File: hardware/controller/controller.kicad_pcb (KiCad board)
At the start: 4 copper layers, 70 x 55 mm, 105 parts, among them SW1 EVP-ASAC1A, SW2 CL-SB-13A-02T, SW3 EVP-ASAC1A, SW4 EVP-ASAC1A, SW5 EVP-ASAC1A, SW6 EVP-ASAC1A, U1 EA8212HT6R, U2 MT3406, U3 XDJK-0051-025, U4 EMS4000RSW, U5 baochip1x, U6 EMS4000RSW, U7 baochip1x, Y1 48 MHz, Y2 48 MHz

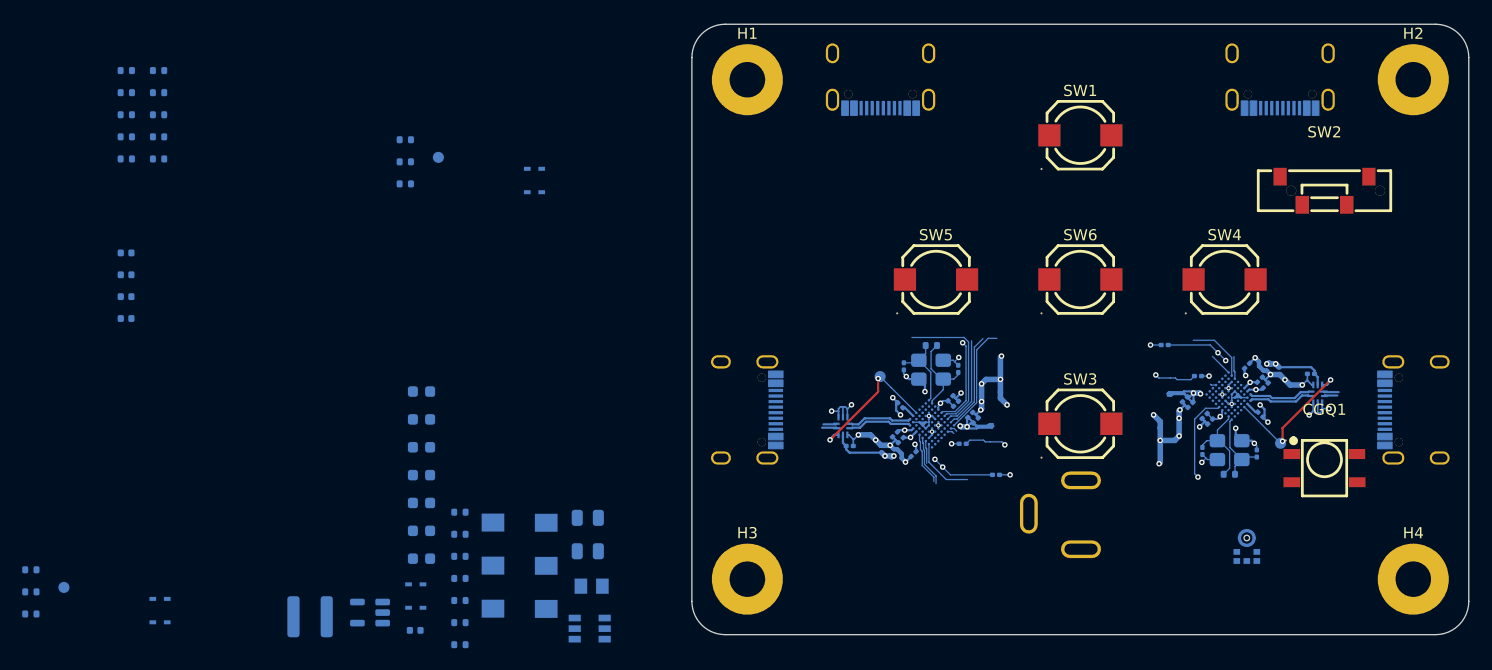
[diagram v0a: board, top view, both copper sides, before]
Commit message: placing power parts
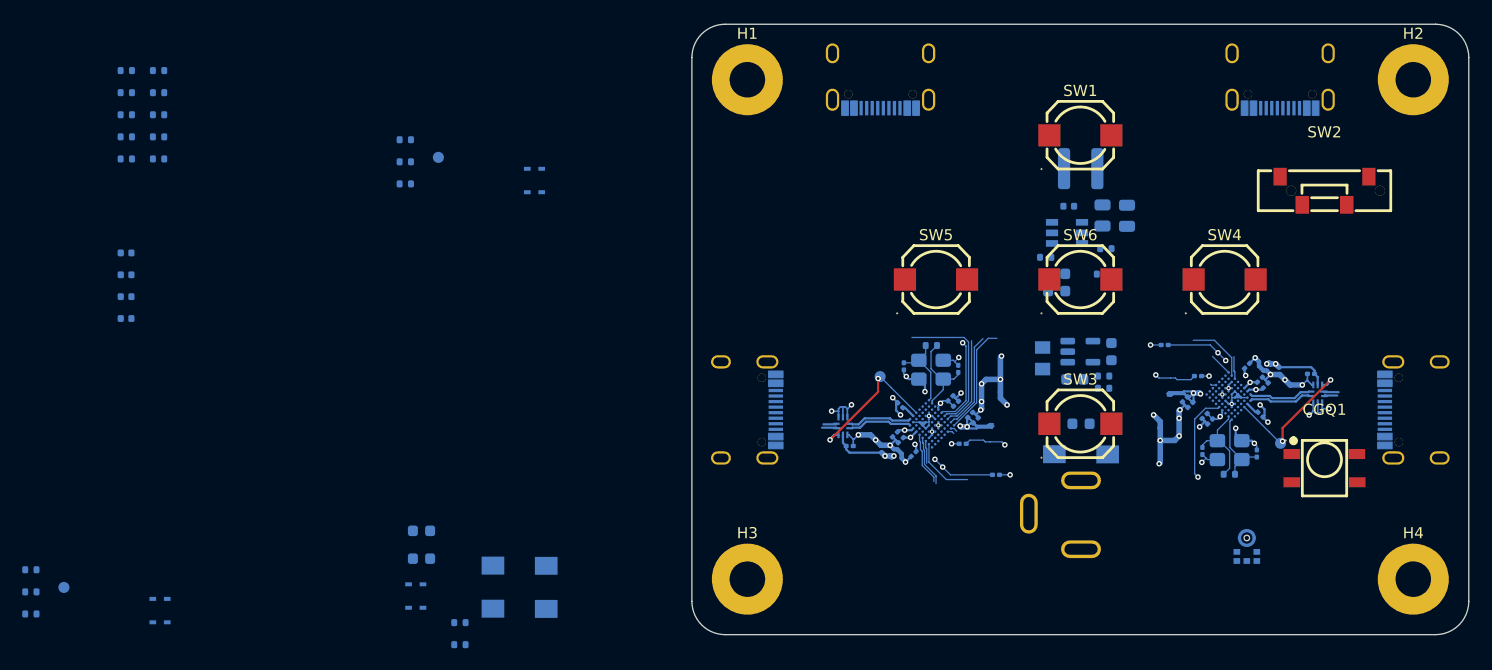
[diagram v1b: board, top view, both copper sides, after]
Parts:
- moved L2 80.3 mm to (135.0, 93.0), turned to 0 degrees
- moved C2 70.2 mm to (134.0, 96.4)
- moved U2 68.2 mm to (135.0, 109.5), turned to 0 degrees
- moved R2 63.6 mm to (137.3, 100.2), turned to 0 degrees
- moved C3 62.5 mm to (137.8, 109.5), turned to -90 degrees
- moved R1 61.7 mm to (137.0, 102.5), turned to 0 degrees
- moved R5 61.2 mm to (131.9, 101.0)
- moved R4 60.8 mm to (137.1, 111.7), turned to 0 degrees
- moved R3 59.9 mm to (137.1, 112.8)
- moved C8 59.8 mm to (135.1, 116.0), turned to 0 degrees
- moved C6 59.6 mm to (132.9, 104.0), turned to 0 degrees
- moved C4 59.3 mm to (132.9, 102.5), turned to 0 degrees
- moved C1 58.9 mm to (134.5, 112.0), turned to 0 degrees
- moved C7 57.2 mm to (139.2, 97.3), turned to -90 degrees
- moved U1 55.9 mm to (133.8, 98.8), turned to 0 degrees
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
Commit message: placing the remaining parts
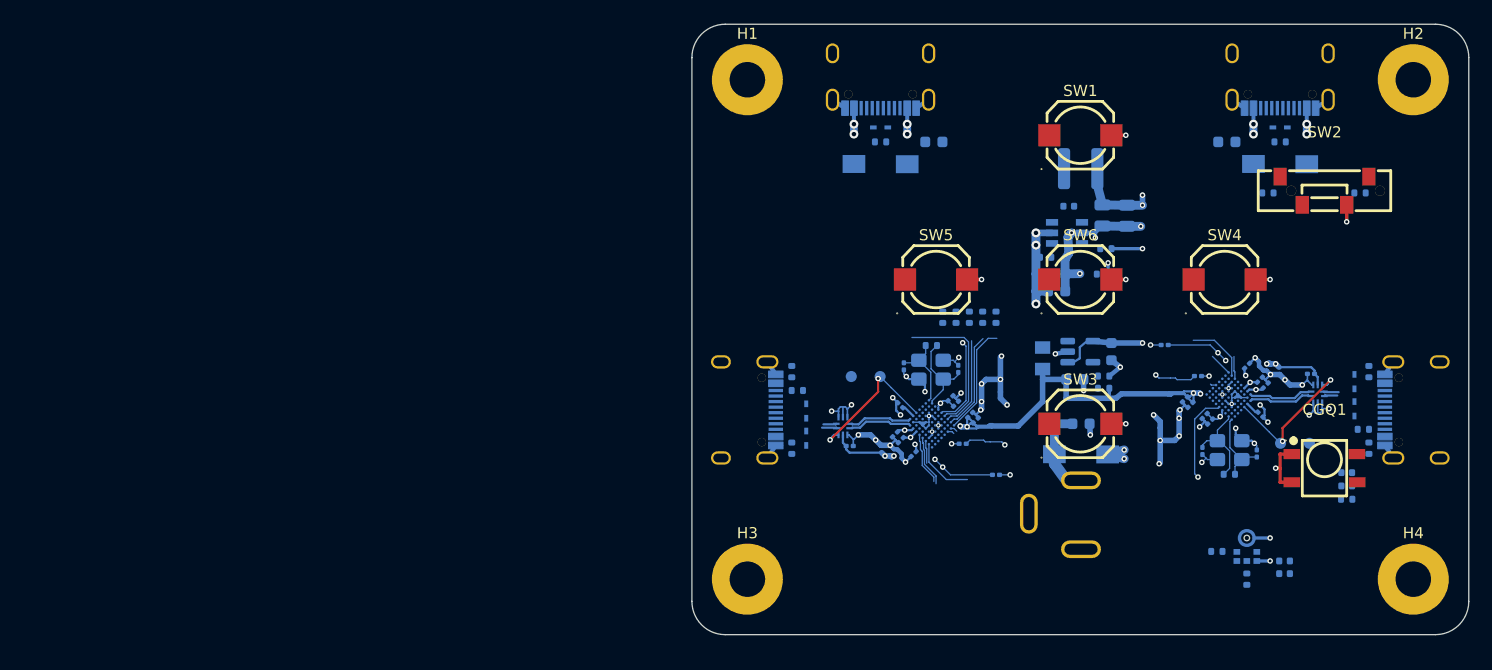
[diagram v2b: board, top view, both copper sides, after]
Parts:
- moved R20 115.3 mm to (159.0, 122.8)
- moved C37 111.1 mm to (159.0, 120.4)
- moved C38 111.0 mm to (159.0, 121.6), turned to 0 degrees
- moved R19 110.1 mm to (150.0, 130.0), turned to 90 degrees
- moved R25 108.5 mm to (160.2, 95.2)
- moved C35 108.3 mm to (153.4, 129.5), turned to 0 degrees
- moved C36 107.5 mm to (153.4, 128.4), turned to 0 degrees
- moved R18 107.4 mm to (147.3, 127.5), turned to 0 degrees
- moved R22 102.9 mm to (151.9, 95.2), turned to 0 degrees
- moved R15 91.2 mm to (161.0, 118.2), turned to 90 degrees
- moved R17 89.1 mm to (160.5, 116.5), turned to 0 degrees
- moved D4 89.1 mm to (153.0, 89.3)
- moved R16 88.9 mm to (161.0, 111.3), turned to -90 degrees
- moved R7 86.7 mm to (153.0, 90.6), turned to 0 degrees
- moved TP4 82.6 mm to (155.6, 117.8)
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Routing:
- net GND: track 78.1 -> 124.5 mm, vias 40 -> 58
- net +12V: track 0.00 -> 26.6 mm, vias 0 -> 11
- net +0.85V: track 30.0 -> 52.2 mm
- net +3.3V: track 60.3 -> 79.2 mm, vias 16 -> 22
- added copper zone on In1.Cu, net +12V
- added copper zone on In1.Cu, net +3.3V

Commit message: finishing the ground and power routing
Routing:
- net GND: track 124.5 -> 153.9 mm, vias 58 -> 78
- net +3.3V: track 79.2 -> 92.7 mm, vias 22 -> 25
- net +12V: track 26.6 -> 35.8 mm

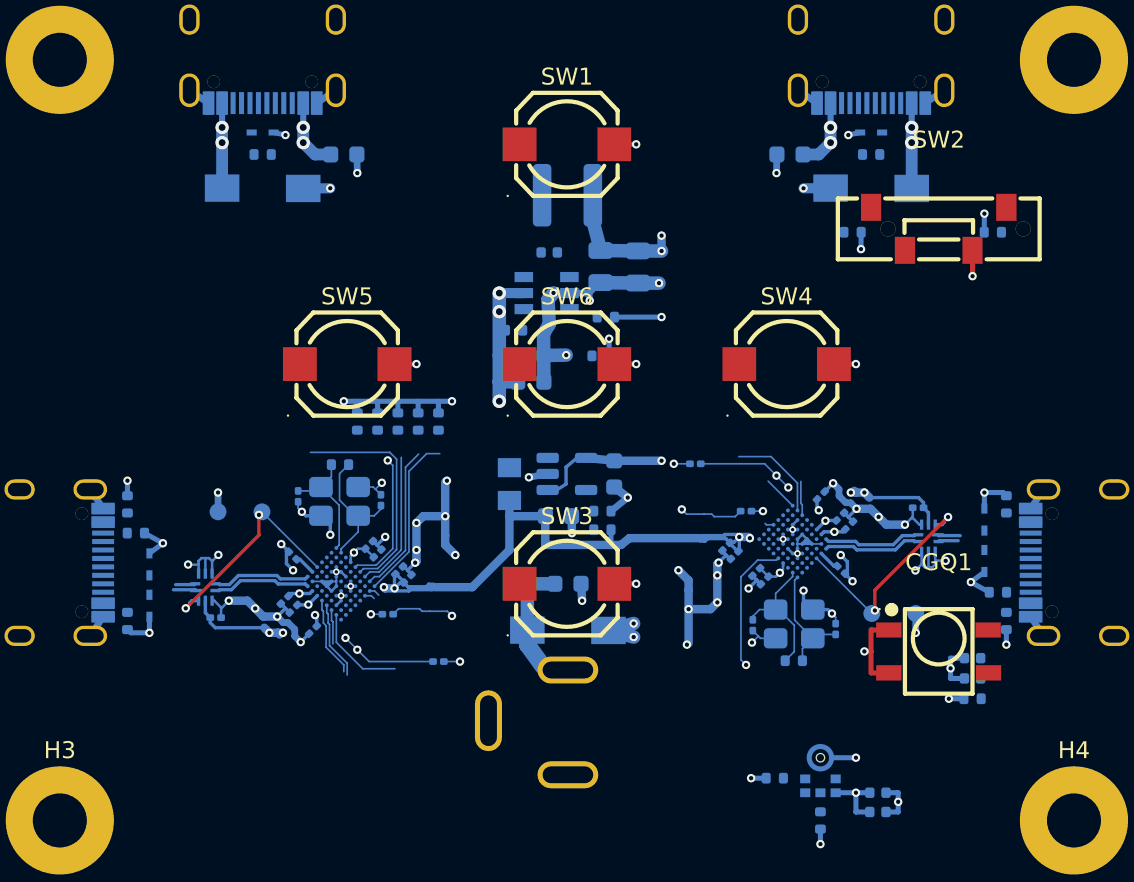
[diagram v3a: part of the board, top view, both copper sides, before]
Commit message: routing some of the shorter paths
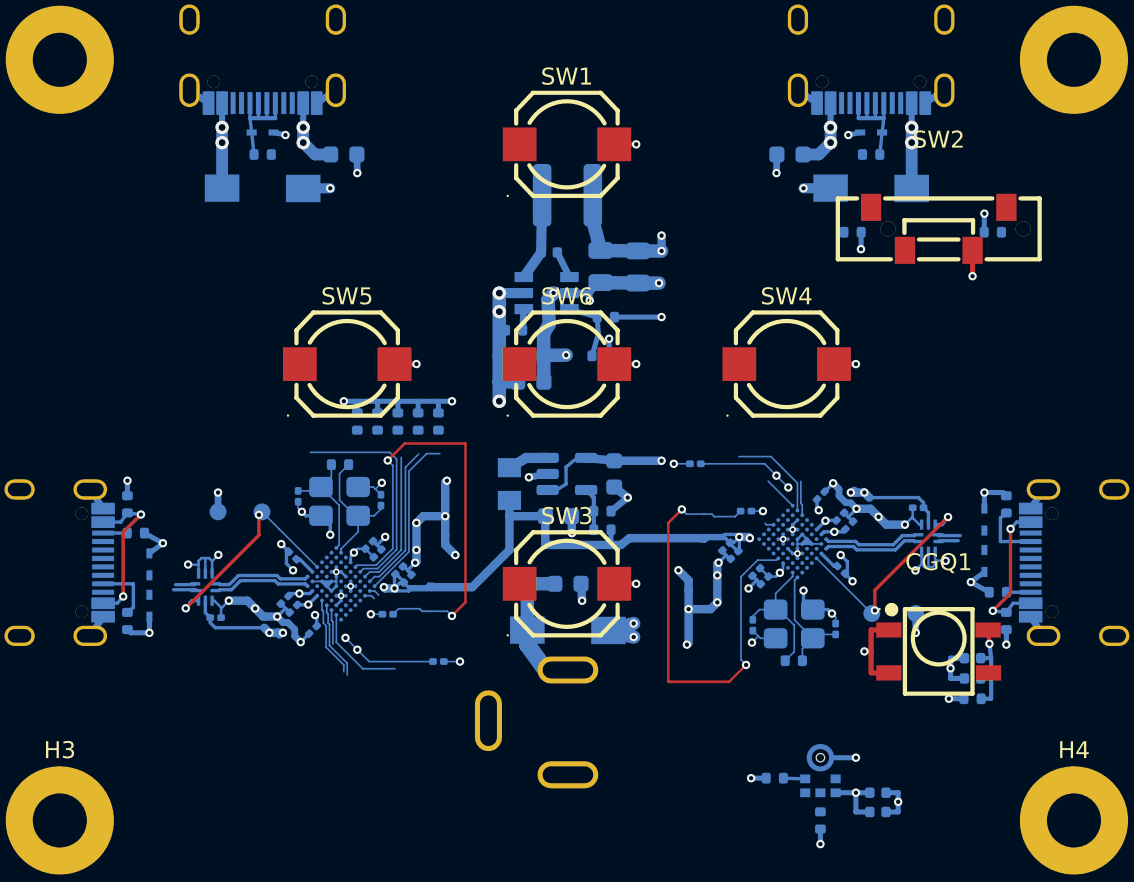
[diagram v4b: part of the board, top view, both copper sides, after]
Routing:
- net Net-(U5B-AORSTn): track 15.6 -> 31.2 mm
- net Net-(U7B-AORSTn): track 15.6 -> 31.2 mm
- net Net-(R15-Pad2): track 0.00 -> 9.17 mm, vias 0 -> 2
- net Net-(R10-Pad2): track 0.00 -> 9.17 mm, vias 0 -> 2
- net Net-(D4-C): track 0.00 -> 7.22 mm
- net Net-(D1-C): track 0.00 -> 7.22 mm
- net Net-(CGQ1-VCC): track 0.00 -> 5.91 mm, vias 0 -> 1
- net Net-(U1-SWITCH): track 0.00 -> 5.16 mm
- net Net-(U1-FBK): track 0.00 -> 4.06 mm
- net Net-(USBC4-CC1): track 0.00 -> 3.64 mm
- net Net-(USBC3-CC1): track 0.00 -> 3.64 mm
- net Net-(U2-FB): track 0.00 -> 2.54 mm
- net Net-(U2-SW): track 0.00 -> 2.42 mm
- net Net-(U1-BOOT): track 0.00 -> 1.62 mm
- net Net-(USBC4-CC2): track 0.00 -> 1.43 mm
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
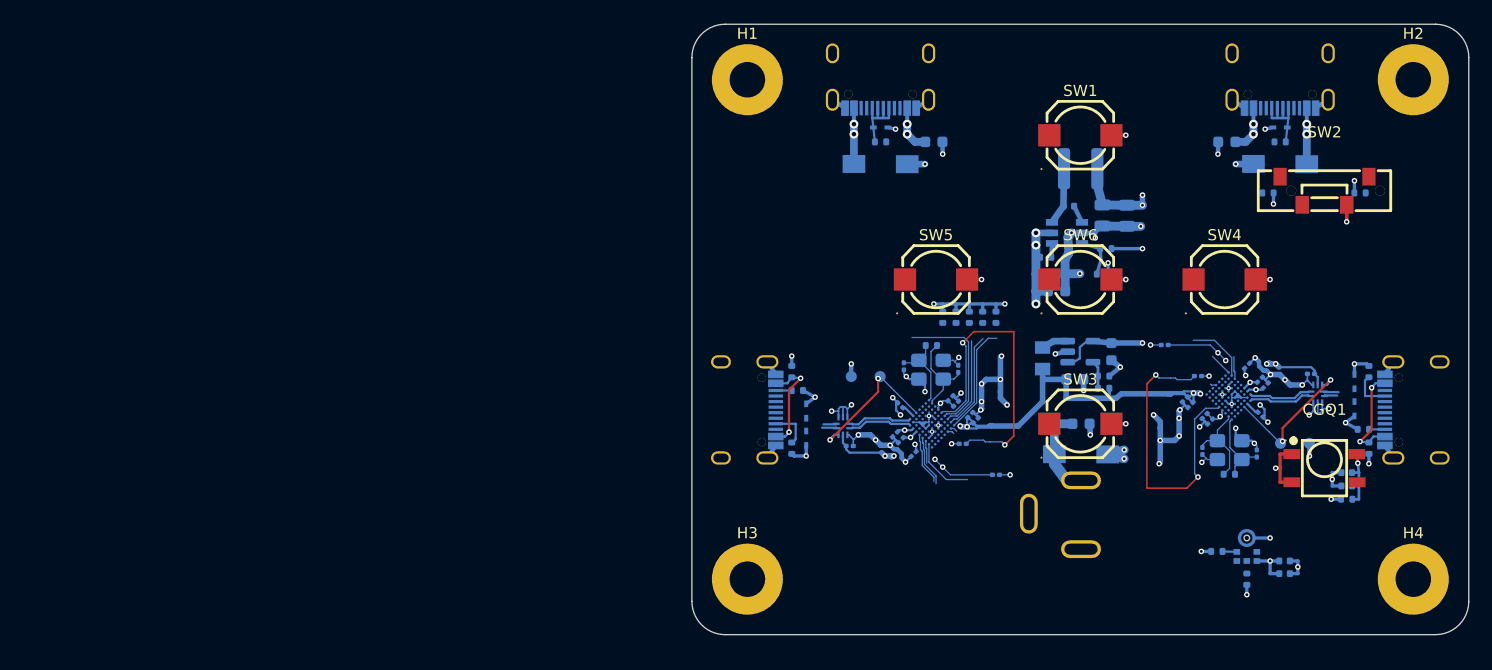
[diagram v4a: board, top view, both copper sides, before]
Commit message: everything routed
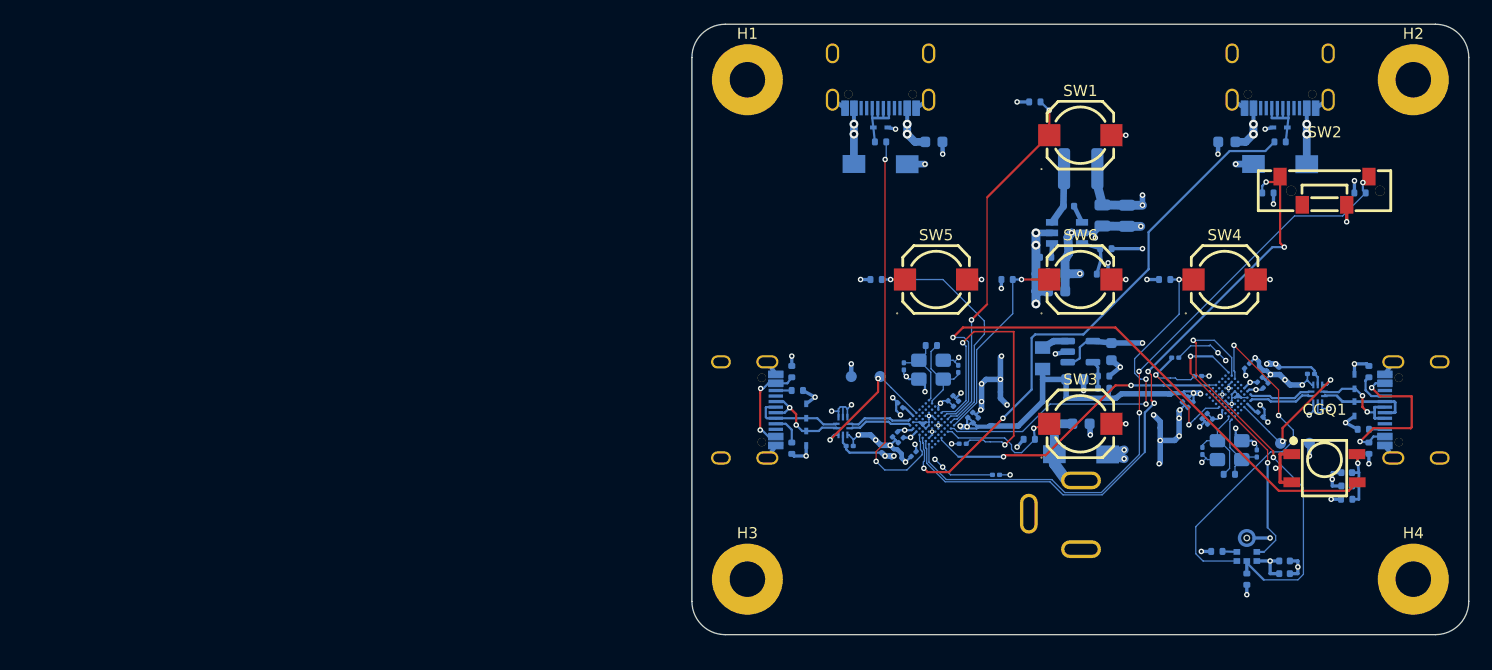
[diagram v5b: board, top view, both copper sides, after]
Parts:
- moved R21 20.7 mm to (130.9, 87.0), turned to 0 degrees
- moved R24 20.3 mm to (142.6, 103.0), turned to 0 degrees
- moved R23 12.3 mm to (130.4, 117.4), turned to 0 degrees
- moved R26 10.2 mm to (116.6, 103.0), turned to 0 degrees
- moved R27 3.54 mm to (128.4, 103.0), turned to 0 degrees
- moved R13 1.49 mm to (143.5, 110.0)
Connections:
- U5 pad A5: LED_DATA_2 -> LED_DATA_1
- U5 pad A6: LED_DATA_1 -> LED_DATA_2
- U5 pad F9: BTN UP -> BTN DOWN
- U5 pad H7: BTN DOWN -> BTN UP
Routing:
- net SOUND REACTIVE ON: track 2.04 -> 58.3 mm, vias 0 -> 4
- net SOUND REACTIVE OFF: track 5.74 -> 59.5 mm, vias 0 -> 3
- net LED_DATA_2: track 4.74 -> 51.6 mm, vias 0 -> 2
- net IR SENSOR DATA: track 13.3 -> 52.8 mm, vias 0 -> 1
- net BTN RIGHT: track 0.63 -> 34.4 mm, vias 0 -> 3
- net BTN UP: track 0.61 -> 33.0 mm, vias 0 -> 2
- net MIC DATA OUTPUT: track 5.74 -> 38.2 mm, vias 0 -> 2
- net LED_DATA_1: track 4.63 -> 36.1 mm, vias 0 -> 2
- net MIC WS: track 2.04 -> 32.3 mm, vias 0 -> 2
- net AUDIO_LINK: track 0.54 -> 28.2 mm, vias 0 -> 2
- net MIC CLOCK: track 2.06 -> 25.9 mm, vias 0 -> 2
- net Net-(U7B-AORSTn): track 31.2 -> 15.1 mm, vias 3 -> 2
- net BTN LEFT: track 8.90 -> 23.4 mm, vias 0 -> 1
- net BTN CENTER: track 9.90 -> 18.6 mm, vias 0 -> 1
- net EAR_DATA_D+: track 1.35 -> 9.01 mm, vias 0 -> 2
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
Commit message: routing adjustments/fixes
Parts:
- moved R25 47.3 mm to (113.0, 97.6)
- moved R22 46.7 mm to (105.3, 97.5), turned to 180 degrees
- moved SW2 46.5 mm to (110.5, 95.0)
- moved R19 23.5 mm to (148.3, 106.6), turned to -90 degrees
- moved R18 23.1 mm to (154.9, 105.8)
- moved MK1 20.1 mm to (156.3, 107.9), turned to -90 degrees
- moved C35 19.6 mm to (153.2, 109.9), turned to 180 degrees
- moved C36 19.5 mm to (153.2, 108.8), turned to 180 degrees
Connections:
- U5 pad A5: LED_DATA_1 -> unconnected-(U5C-PB5-PadA5)
- U5 pad A6: LED_DATA_2 -> unconnected-(U5C-PB4-PadA6)
- U5 pad A7: SOUND REACTIVE ON -> unconnected-(U5C-PB3-PadA7)
- U5 pad A8: SOUND REACTIVE OFF -> unconnected-(U5C-PB2-PadA8)
- U5 pad E1: unconnected-(U5D-PC12-PadE1) -> SOUND REACTIVE ON
- U5 pad F1: unconnected-(U5D-PC11-PadF1) -> SOUND REACTIVE OFF
- U5 pad G1: unconnected-(U5D-PC10-PadG1) -> LED_DATA_1
- U5 pad H3: unconnected-(U5D-PC9-PadH3) -> LED_DATA_2
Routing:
- net SOUND REACTIVE OFF: track 59.5 -> 24.2 mm, vias 3 -> 1
- net SOUND REACTIVE ON: track 58.3 -> 32.7 mm, vias 4 -> 1
- net MIC DATA OUTPUT: track 38.2 -> 12.7 mm, vias 2 -> 0
- net MIC WS: track 32.3 -> 9.92 mm
- net Net-(U5B-AORSTn): track 31.2 -> 18.5 mm
- net LED_DATA_1: track 36.1 -> 25.2 mm
- net LED_DATA_2: track 51.6 -> 44.2 mm
- net MIC CLOCK: track 25.9 -> 19.9 mm
- net GND: track 153.9 -> 152.6 mm
- net +3.3V: track 87.2 -> 86.2 mm, vias 28 -> 27
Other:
- board text added: "OUT TO 1-12"
- board text added: "OUT TO 13-25"
